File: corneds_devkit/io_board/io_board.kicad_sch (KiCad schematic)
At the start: 0 parts

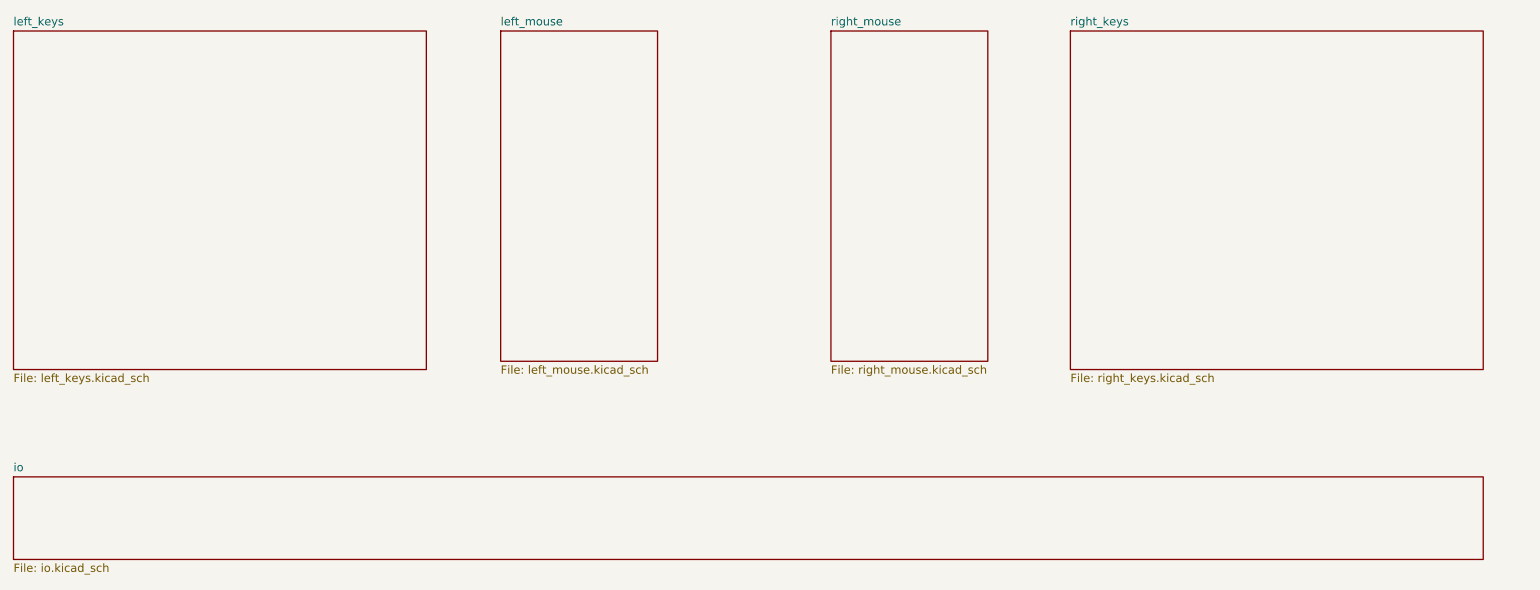
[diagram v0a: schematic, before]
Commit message: re-routed io board with keypad IC
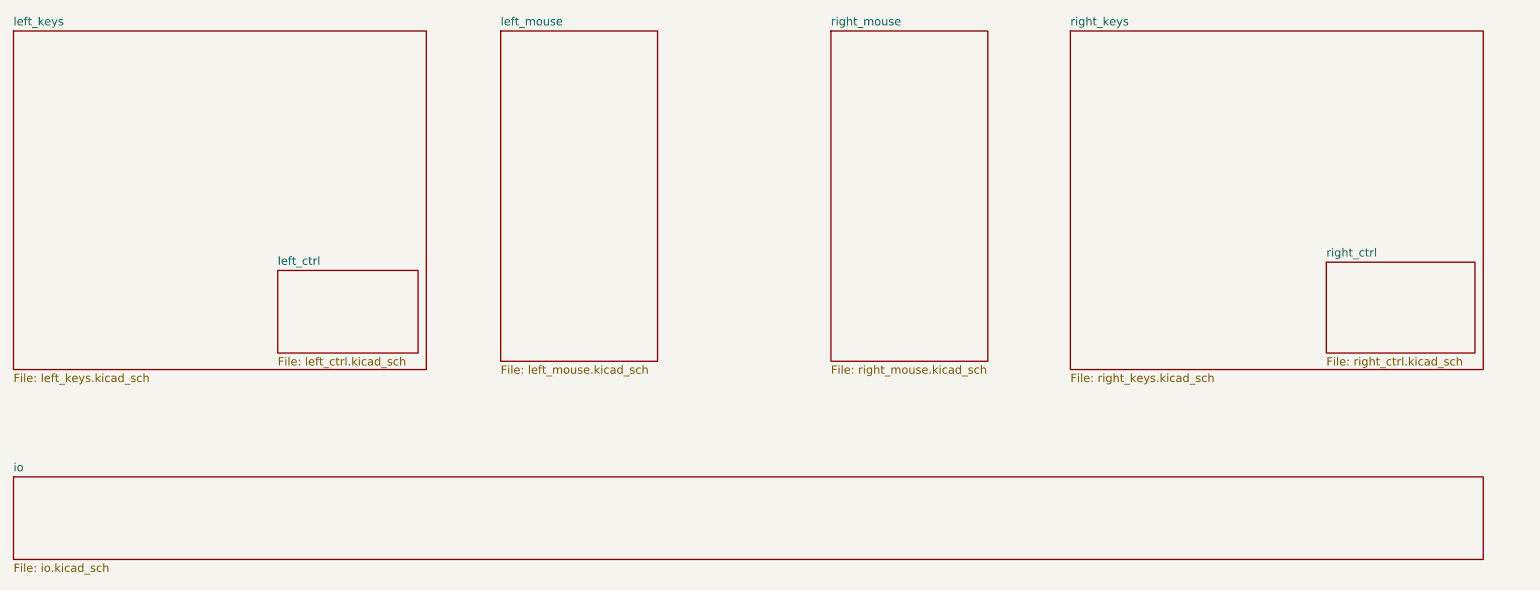
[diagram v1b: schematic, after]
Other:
- added sheet left_ctrl (left_ctrl.kicad_sch)
- added sheet right_ctrl (right_ctrl.kicad_sch)
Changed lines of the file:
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@@
+			(project "io_board"
+				(path "/244b6d6b-132d-4d50-ae86-e41103b29008"
+					(page "8")
+				)
+			)
+		)
+	)
+	(sheet
+		(at 238.76 88.9)
+		(size 22.86 13.97)
+		(fields_autoplaced yes)
+		(stroke
+			(width 0.1524)
+			(type solid)
+		)
+		(fill
+			(color 0 0 0 0.0000)
+		)
+		(property "Sheetname" "right_ctrl"
+			(at 238.76 88.1884 0)
+			(effects
+				(font
+					(size 1.27 1.27)
+				)
+				(justify left bottom)
+			)
+		)
+		(property "Sheetfile" "right_ctrl.kicad_sch"
+			(at 238.76 103.4546 0)
+			(effects
+				(font
+					(size 1.27 1.27)
+				)
+				(justify left top)
+			)
+		)
+		(instances
 			(project "io_board"
 				(path "/244b6d6b-132d-4d50-ae86-e41103b29008"
 					(page "6")
+				)
+			)
+		)
+	)
+	(sheet
+		(at 77.47 90.17)
+		(size 21.59 12.7)
+		(fields_autoplaced yes)
+		(stroke
+			(width 0.1524)
+			(type solid)
+		)
+		(fill
+			(color 0 0 0 0.0000)
+		)
+		(property "Sheetname" "left_ctrl"
+			(at 77.47 89.4584 0)
+			(effects
+				(font
+					(size 1.27 1.27)
+				)
+				(justify left bottom)
+			)
+		)
+		(property "Sheetfile" "left_ctrl.kicad_sch"
+			(at 77.47 103.4546 0)
+			(effects
+				(font
+					(size 1.27 1.27)
+				)
+				(justify left top)
+			)
+		)
+		(instances
+			(project "io_board"
+				(path "/244b6d6b-132d-4d50-ae86-e41103b29008"
+					(page "3")
 				)
 			)
@@
 			(project "io_board"
 				(path "/244b6d6b-132d-4d50-ae86-e41103b29008"
-					(page "3")
+					(page "5")
 				)
 			)
@@
 			(project "io_board"
 				(path "/244b6d6b-132d-4d50-ae86-e41103b29008"
-					(page "5")
+					(page "7")
 				)
 			)

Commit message: ordered devkit rev A
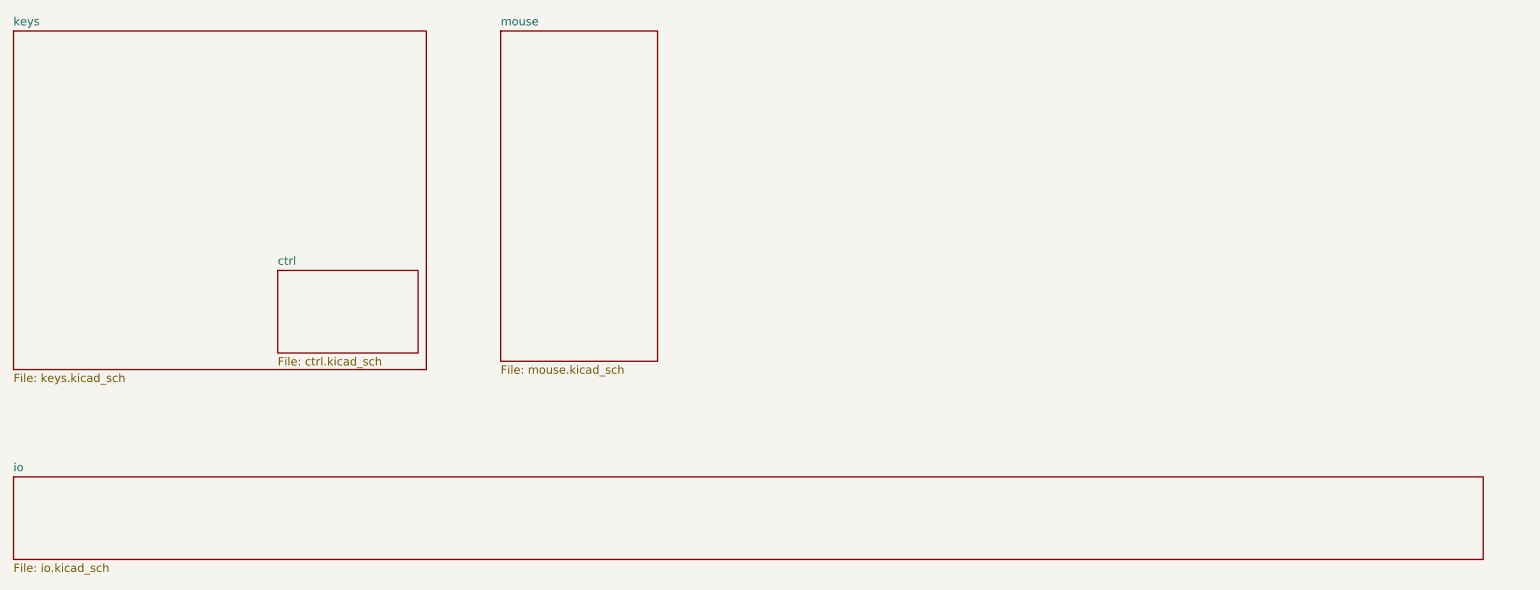
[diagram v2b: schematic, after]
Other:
- sheet left_ctrl renamed ctrl
- sheet left_keys renamed keys
- sheet left_mouse renamed mouse
- removed sheet right_ctrl
- removed sheet right_keys
- removed sheet right_mouse
- sheet ctrl: file left_ctrl.kicad_sch -> ctrl.kicad_sch
- sheet keys: file left_keys.kicad_sch -> keys.kicad_sch
- sheet mouse: file left_mouse.kicad_sch -> mouse.kicad_sch
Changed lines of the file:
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@@
 			(color 0 0 0 0.0000)
 		)
-		(property "Sheetname" "left_keys"
+		(property "Sheetname" "keys"
 			(at 36.83 52.6284 0)
 			(effects
@@
 			)
 		)
-		(property "Sheetfile" "left_keys.kicad_sch"
+		(property "Sheetfile" "keys.kicad_sch"
 			(at 36.83 105.9946 0)
 			(effects
@@
 	)
 	(sheet
-		(at 238.76 88.9)
-		(size 22.86 13.97)
-		(fields_autoplaced yes)
-		(stroke
-			(width 0.1524)
-			(type solid)
-		)
-		(fill
-			(color 0 0 0 0.0000)
-		)
-		(property "Sheetname" "right_ctrl"
-			(at 238.76 88.1884 0)
-			(effects
-				(font
-					(size 1.27 1.27)
-				)
-				(justify left bottom)
-			)
-		)
-		(property "Sheetfile" "right_ctrl.kicad_sch"
-			(at 238.76 103.4546 0)
-			(effects
-				(font
-					(size 1.27 1.27)
-				)
-				(justify left top)
-			)
-		)
-		(instances
-			(project "io_board"
-				(path "/244b6d6b-132d-4d50-ae86-e41103b29008"
-					(page "6")
-				)
-			)
-		)
-	)
-	(sheet
 		(at 77.47 90.17)
 		(size 21.59 12.7)
@@
 			(color 0 0 0 0.0000)
 		)
-		(property "Sheetname" "left_ctrl"
+		(property "Sheetname" "ctrl"
 			(at 77.47 89.4584 0)
 			(effects
@@
 			)
 		)
-		(property "Sheetfile" "left_ctrl.kicad_sch"
+		(property "Sheetfile" "ctrl.kicad_sch"
 			(at 77.47 103.4546 0)
 			(effects
@@
 	)
 	(sheet
-		(at 199.39 53.34)
-		(size 63.5 52.07)
-		(fields_autoplaced yes)
-		(stroke
-			(width 0.1524)
-			(type solid)
-		)
-		(fill
-			(color 0 0 0 0.0000)
-		)
-		(property "Sheetname" "right_keys"
-			(at 199.39 52.6284 0)
-			(effects
-				(font
-					(size 1.27 1.27)
-				)
-				(justify left bottom)
-			)
-		)
-		(property "Sheetfile" "right_keys.kicad_sch"
-			(at 199.39 105.9946 0)
-			(effects
-				(font
-					(size 1.27 1.27)
-				)
-				(justify left top)
-			)
-		)
-		(instances
-			(project "io_board"
-				(path "/244b6d6b-132d-4d50-ae86-e41103b29008"
-					(page "5")
-				)
-			)
-		)
-	)
-	(sheet
-		(at 162.56 53.34)
-		(size 24.13 50.8)
-		(fields_autoplaced yes)
-		(stroke
-			(width 0.1524)
-			(type solid)
-		)
-		(fill
-			(color 0 0 0 0.0000)
-		)
-		(property "Sheetname" "right_mouse"
-			(at 162.56 52.6284 0)
-			(effects
-				(font
-					(size 1.27 1.27)
-				)
-				(justify left bottom)
-			)
-		)
-		(property "Sheetfile" "right_mouse.kicad_sch"
-			(at 162.56 104.7246 0)
-			(effects
-				(font
-					(size 1.27 1.27)
-				)
-				(justify left top)
-			)
-		)
-		(instances
-			(project "io_board"
-				(path "/244b6d6b-132d-4d50-ae86-e41103b29008"
-					(page "7")
-				)
-			)
-		)
-	)
-	(sheet
 		(at 111.76 53.34)
 		(size 24.13 50.8)
@@
 			(color 0 0 0 0.0000)
 		)
-		(property "Sheetname" "left_mouse"
+		(property "Sheetname" "mouse"
 			(at 111.76 52.6284 0)
 			(effects
@@
 			)
 		)
-		(property "Sheetfile" "left_mouse.kicad_sch"
+		(property "Sheetfile" "mouse.kicad_sch"
 			(at 111.76 104.7246 0)
 			(effects
